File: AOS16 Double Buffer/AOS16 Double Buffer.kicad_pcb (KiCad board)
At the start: 4 copper layers, 50 x 75 mm, 69 parts, among them IC1 SN74AHCT16245DGVR, IC2 SN74AHCT16245DGVR, IC3 SN74AHCT16245DGVR, IC4 SN74AHCT16245DGVR, J1 Conn_01x07_Pin, J2 Conn_02x08_Top_Bottom, J3 Conn_02x08_Top_Bottom, J4 Conn_02x08_Top_Bottom, J5 Conn_02x08_Top_Bottom, U1 74AHCT1G08, U2 74AHCT1G08, U3 74AHCT1G32, U4 74AHCT1G32, U5 74AHCT1G04, U6 74AHCT1G04, U7 74LVC157, U8 71016S12PHG8

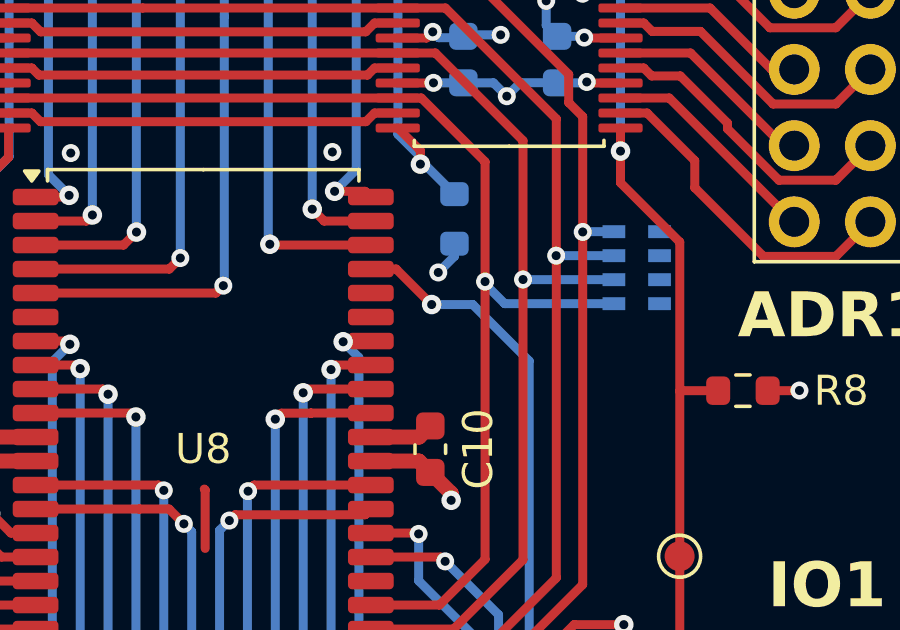
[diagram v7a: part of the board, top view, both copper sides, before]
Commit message: Fixed ERC errors
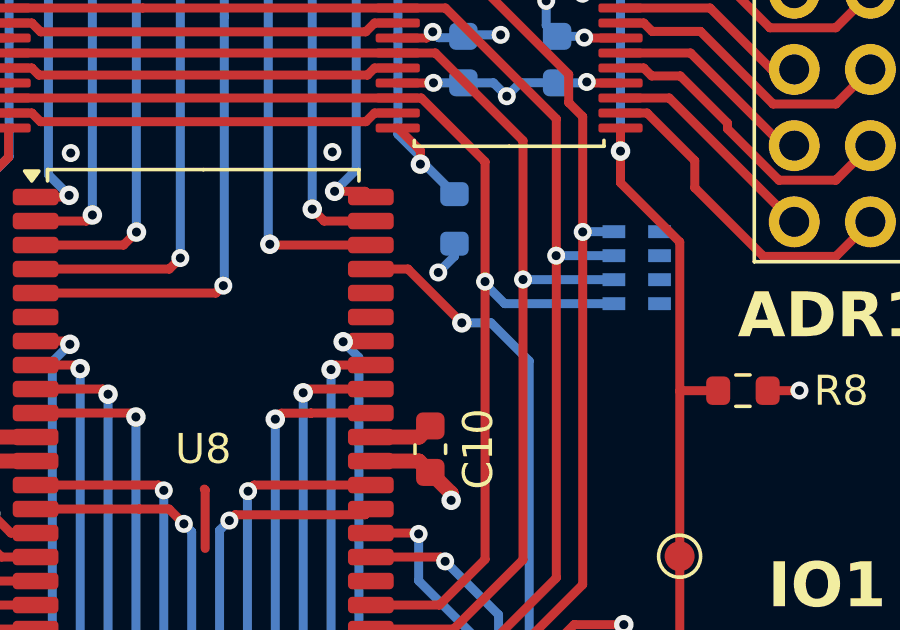
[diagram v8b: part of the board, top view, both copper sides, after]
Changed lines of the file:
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@@
 	)
 	(segment
-		(start 153.15625 72.47625)
-		(end 152.3125 72.47625)
+		(start 155.345 74.27)
+		(end 153.55125 72.47625)
 		(width 0.3)
 		(layer "F.Cu")
@@
 	)
 	(segment
-		(start 154.34 73.66)
-		(end 153.15625 72.47625)
+		(start 153.55125 72.47625)
+		(end 152.3125 72.47625)
 		(width 0.3)
 		(layer "F.Cu")
@@
 	)
 	(via
-		(at 154.34 73.66)
+		(at 155.345 74.27)
 		(size 0.65)
 		(drill 0.3)
@@
 	)
 	(segment
-		(start 157.59 75.54)
-		(end 157.59 98.88)
+		(start 157.59 98.88)
+		(end 154.435 102.035)
+		(width 0.3)
+		(layer "B.Cu")
+		(net 74)
+	)
+	(segment
+		(start 155.345 74.27)
+		(end 156.32 74.27)
 		(width 0.3)
 		(layer "B.Cu")
@@
 		(start 154.435 115.025)
 		(end 154.435 114.995)
-		(width 0.3)
-		(layer "B.Cu")
-		(net 74)
-	)
-	(segment
-		(start 154.435 102.035)
-		(end 154.435 114.995)
-		(width 0.3)
-		(layer "B.Cu")
-		(net 74)
-	)
-	(segment
-		(start 157.59 98.88)
-		(end 154.435 102.035)
-		(width 0.3)
-		(layer "B.Cu")
-		(net 74)
-	)
-	(segment
-		(start 154.34 73.66)
-		(end 155.71 73.66)
-		(width 0.3)
-		(layer "B.Cu")
-		(net 74)
-	)
-	(segment
-		(start 155.71 73.66)
-		(end 157.59 75.54)
 		(width 0.3)
 		(layer "B.Cu")
@@
 		(width 0.3)
 		(layer "B.Cu")
+		(net 74)
+	)
+	(segment
+		(start 157.59 75.54)
+		(end 157.59 98.88)
+		(width 0.3)
+		(layer "B.Cu")
+		(net 74)
+	)
+	(segment
+		(start 156.32 74.27)
+		(end 157.59 75.54)
+		(width 0.3)
+		(layer "B.Cu")
+		(net 74)
+	)
+	(segment
+		(start 154.435 102.035)
+		(end 154.435 114.995)
+		(width 0.3)
+		(layer "B.Cu")
